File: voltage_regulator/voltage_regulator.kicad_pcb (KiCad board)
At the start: 2 copper layers, 47.7 x 18.6 mm, 19 parts, among them J1 Conn_01x05_Male, U1 TPS54331DR

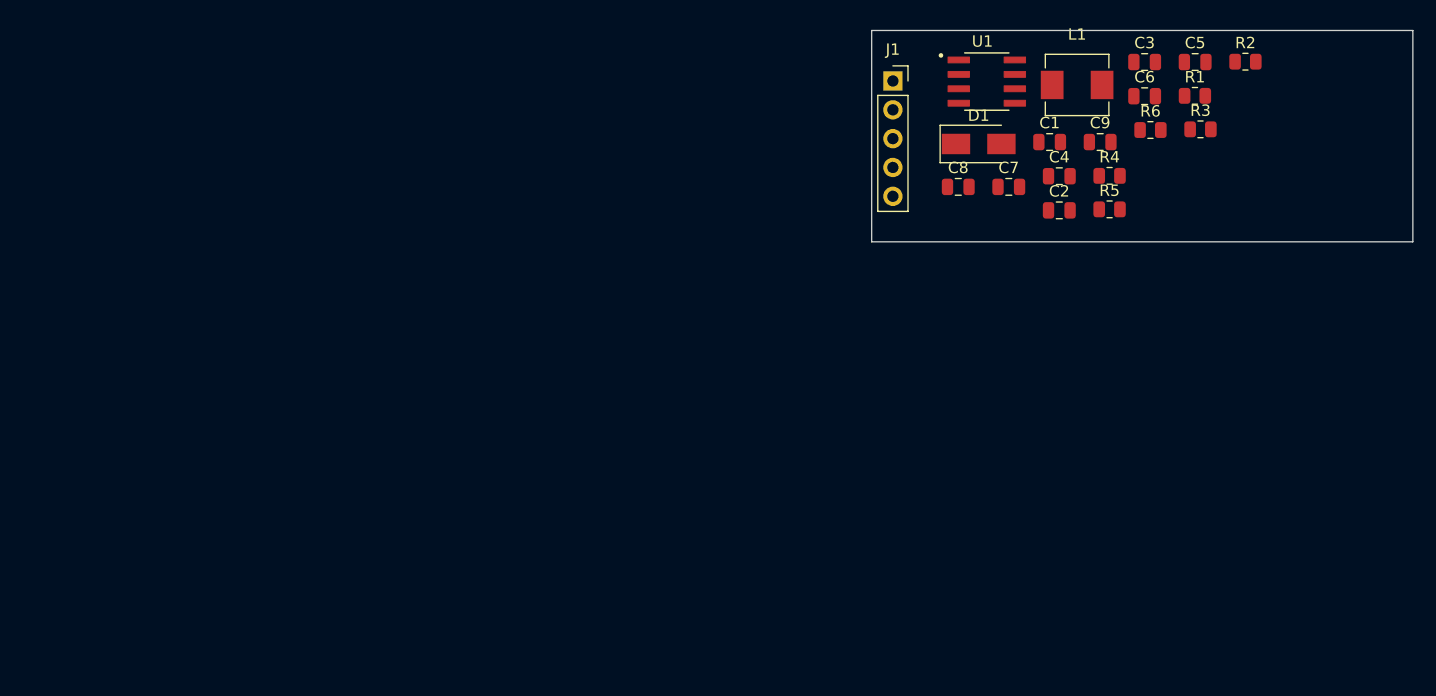
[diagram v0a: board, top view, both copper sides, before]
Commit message: Updated layout
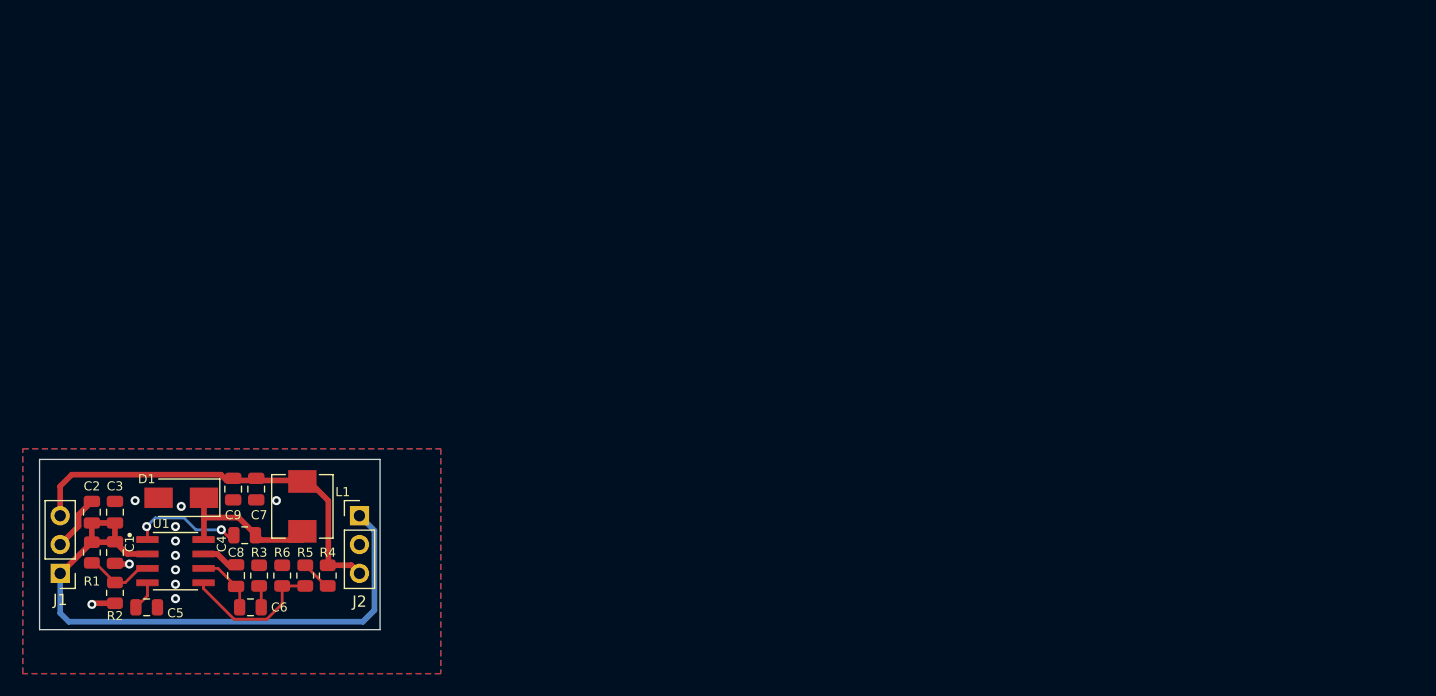
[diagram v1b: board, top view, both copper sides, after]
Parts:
- added J2: Conn_01x03_Male, Connector_PinHeader_2.54mm:PinHeader_1x03_P2.54mm_Vertical, F.Cu at (78.2, 105.0)
- added REF**: OSHW-Symbol_6.7x6mm_SilkScreen, Symbol:OSHW-Symbol_6.7x6mm_SilkScreen, B.Cu at (65.0, 109.7)
- J1: value Conn_01x05_Male -> Conn_01x03_Male; footprint Connector_PinSocket_2.54mm:PinSocket_1x05_P2.54mm_Vertical -> Connector_PinHeader_2.54mm:PinHeader_1x03_P2.54mm_Vertical
- moved R2 110.0 mm to (56.6, 111.8), turned to -90 degrees
- moved R1 105.2 mm to (54.6, 108.2), turned to -90 degrees
- moved C5 104.1 mm to (59.4, 113.0)
- moved C3 99.0 mm to (56.6, 104.6), turned to 90 degrees
- moved R3 91.8 mm to (69.3, 110.2), turned to 90 degrees
- moved C6 90.7 mm to (68.6, 113.0)
- moved C1 89.9 mm to (56.6, 108.2), turned to -90 degrees
- moved C2 89.3 mm to (54.6, 104.6), turned to 90 degrees
- moved R6 86.0 mm to (71.4, 110.2), turned to 90 degrees
- moved J1 85.2 mm to (51.8, 110.0), turned to 180 degrees
- moved U1 83.0 mm to (62.0, 109.0)
- moved C9 82.3 mm to (67.1, 102.6), turned to -90 degrees
- moved C4 78.4 mm to (68.1, 106.7), turned to 180 degrees
- moved R5 77.9 mm to (73.4, 110.2), turned to -90 degrees
- moved L1 77.7 mm to (73.2, 104.1), turned to 90 degrees
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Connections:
- J1 pad 1: +5V -> +12V
- J1 pad 2: +12V -> GND
- J1 pad 3: GND -> +5V
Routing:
- net +12V: track 0.00 -> 55.5 mm
- net +5V: track 0.00 -> 36.3 mm
- net Net-(C4-Pad1): track 0.00 -> 13.2 mm
- net Net-(R5-Pad2): track 0.00 -> 12.7 mm
- net GND: track 0.00 -> 11.6 mm, vias 0 -> 11
- net Net-(C4-Pad2): track 0.00 -> 10.0 mm, vias 0 -> 2
- net Net-(R1-Pad2): track 0.00 -> 6.13 mm
- net Net-(C6-Pad1): track 0.00 -> 5.50 mm
- net Net-(R4-Pad2): track 0.00 -> 2.79 mm
- net Net-(C5-Pad1): track 0.00 -> 2.58 mm
- net Net-(C6-Pad2): track 0.00 -> 1.96 mm
- added copper zone on B.Cu, net GND
- added copper zone on F.Cu, net GND
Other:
- board size 47.7 x 18.6 mm -> 30 x 15 mm
- board text added: "+12v"
- board text added: "+5v"
- board text added: "12v"
- board text added: "12v to 5v 3A Buck Converter Version 1.0"
- board text added: "5v"
- board text added: "GND"
- board text added: "https://github.com/akuker/hw_projects"
